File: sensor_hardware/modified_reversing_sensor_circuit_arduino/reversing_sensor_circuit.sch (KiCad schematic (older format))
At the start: 0 parts

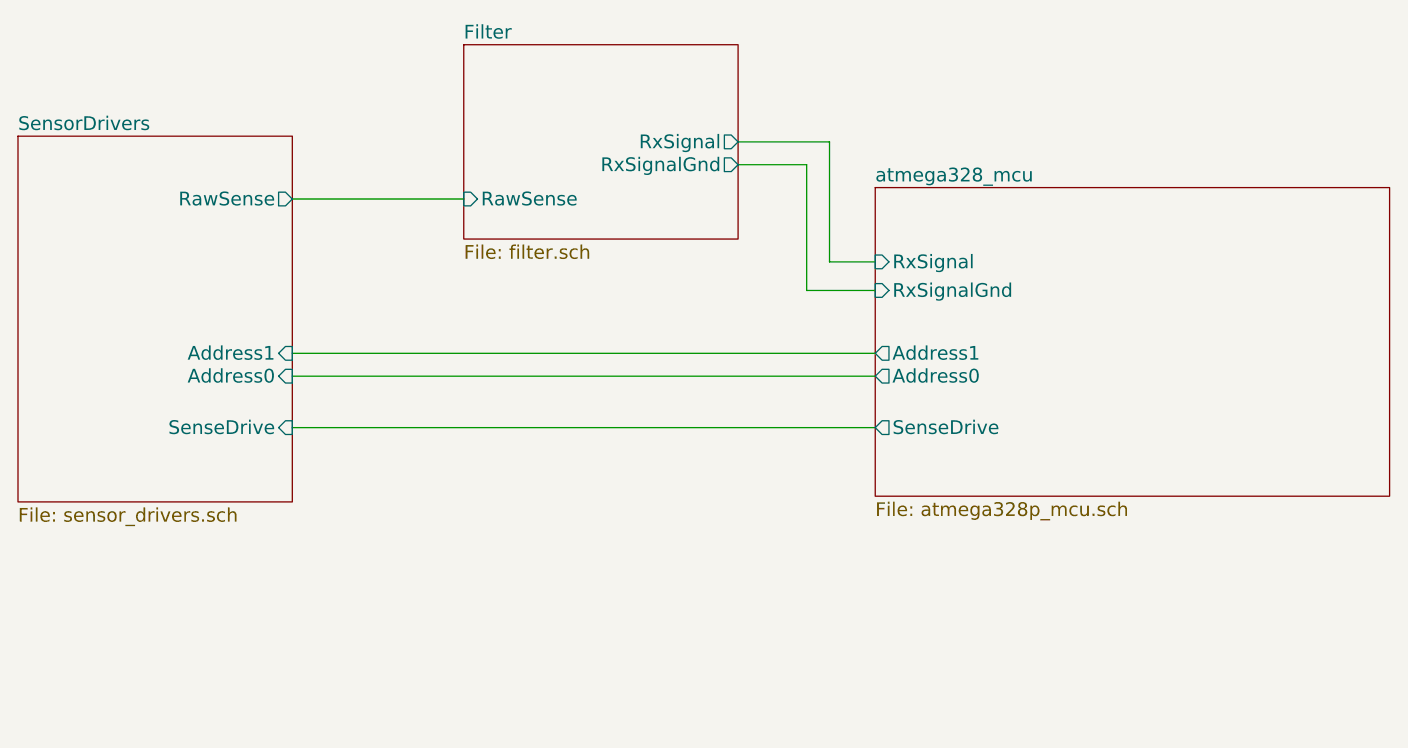
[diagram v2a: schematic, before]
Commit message: update readme and add wifi circuit details
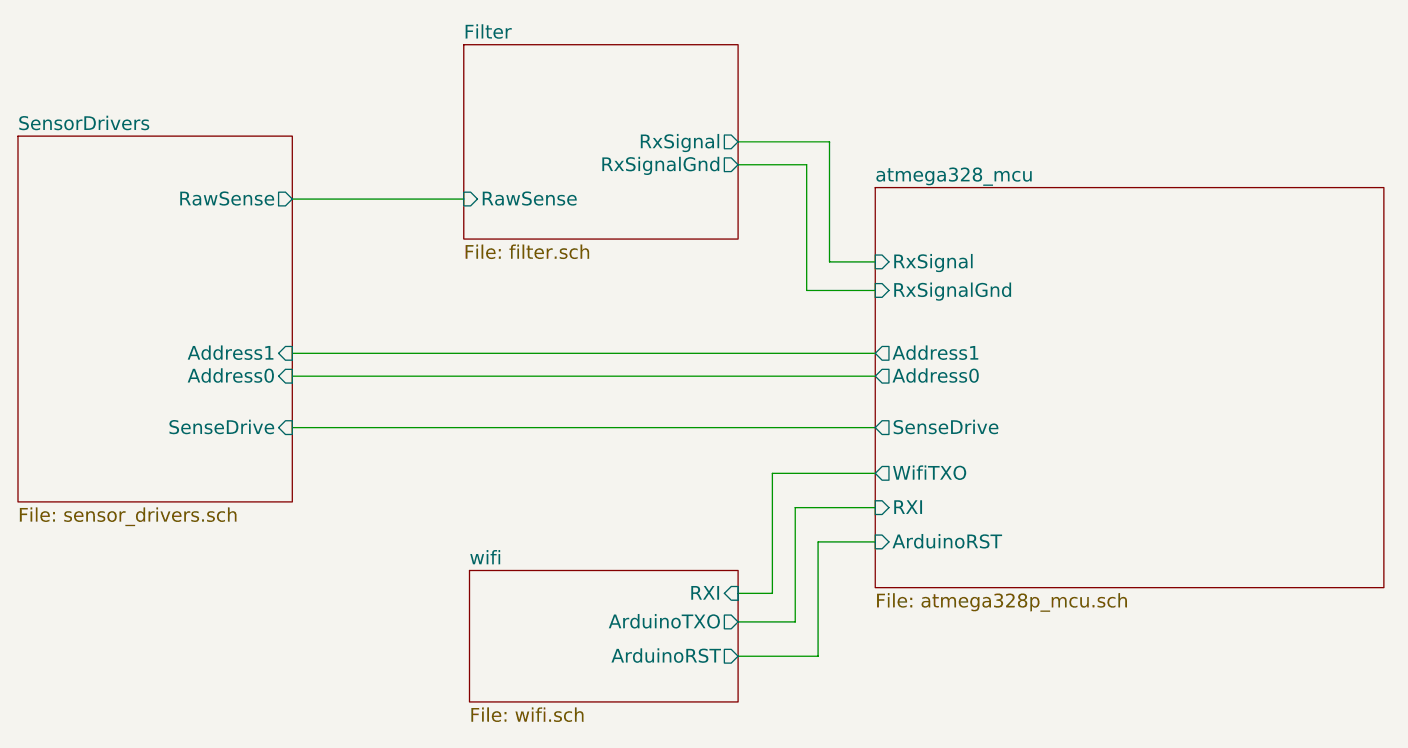
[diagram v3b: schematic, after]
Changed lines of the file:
@@
 LIBS:valves
 LIBS:atmega328p
+LIBS:esp-01
 LIBS:reversing_sensor_circuit-cache
 EELAYER 25 0
@@
 $Descr A4 11693 8268
 encoding utf-8
-Sheet 1 4
+Sheet 1 5
 Title ""
 Date ""
@@
 	4725 2600 3975 2600
 $Sheet
-S 6525 2550 2250 1350
+S 6525 2550 2225 1750
 U 61407FAF
 F0 "atmega328_mcu" 60
@@
 F5 "Address1" O L 6525 3275 60
 F6 "SenseDrive" O L 6525 3600 60
+F7 "ArduinoRST" I L 6525 4100 60
+F8 "WifiTXO" O L 6525 3800 60
+F9 "RXI" I L 6525 3950 60
 $EndSheet
 Wire Wire Line
@@
 Wire Wire Line
 	6525 3275 3975 3275
+$Sheet
+S 4750 4225 1175 575
+U 617533DD
+F0 "wifi" 60
+F1 "wifi.sch" 60
+F2 "RXI" I R 5925 4325 60
+F3 "ArduinoRST" O R 5925 4600 60
+F4 "ArduinoTXO" O R 5925 4450 60
+$EndSheet
+Wire Wire Line
+	5925 4325 6075 4325
+Wire Wire Line
+	6075 4325 6075 3800
+Wire Wire Line
+	6075 3800 6525 3800
+Wire Wire Line
+	6525 3950 6175 3950
+Wire Wire Line
+	6175 3950 6175 4450
+Wire Wire Line
+	6175 4450 5925 4450
+Wire Wire Line
+	5925 4600 6275 4600
+Wire Wire Line
+	6275 4600 6275 4100
+Wire Wire Line
+	6275 4100 6525 4100
 $EndSCHEMATC
